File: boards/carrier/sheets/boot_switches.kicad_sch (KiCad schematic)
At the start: 8 parts, among them SW1 DS-04P, SW2 TS-1002S-06026C

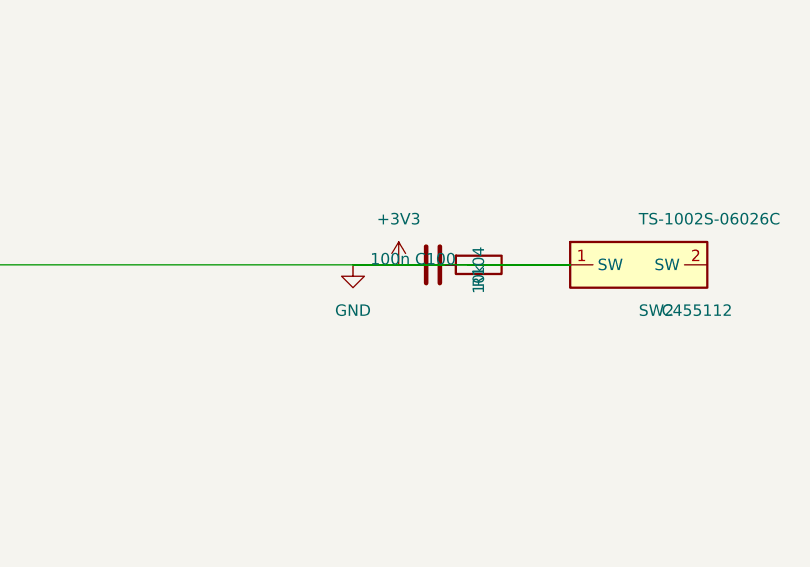
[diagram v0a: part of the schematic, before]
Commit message: Stage 5.5: rotation-derived pin sides + per-edge slot pitch (cluster fix)
Applies the in-flight cluster-fix agent's work (session limit cut its
own commit short). Two architectural changes that close the
sub-sheet wire_dangling / net-merging class of errors:

1) Rotation-derived page-side detection
   (core/layout/geometry.py + core/layout/cluster.py)

   Previously cluster.pin_side() compared abs(pin.x) vs abs(pin.y) on
   the symbol-relative coordinate to guess which body edge a pin
   emerges from. This mis-classified pins on ICs whose pin columns
   span a larger y-range than the body width — FUSB302's seven
   left-column pins (±7.62 mm in y) on a 20 mm-wide body wrap to
   "top/bottom" with the axis-dominance rule, but they're actually
   left-edge pins. The cluster then places passives on the wrong
   side and the resulting wires collide into other nets.

   The new page_side_from_pin() helper derives the page-side from the
   pin's intrinsic KiCad rotation (0 = LEFT edge, 90 = BOTTOM, 180 =
   RIGHT, 270 = TOP) combined with the placed symbol's rotation. This
   is the canonical KiCad convention and doesn't depend on body
   proportions.

   PinGeometry / PinGeometryAbs gain pin_rotation + symbol_rotation
   fields; SymbolGeometryCache reads pin.rotation from the cached
   SymbolDefinition (kicad-sch-api's list_pins() flattens it away).
   pin_side() takes optional pin_rotation/symbol_rotation; falls back
   to the legacy heuristic when not supplied.

2) Per-edge slot pitch
   (core/layout/_constants.py + core/layout/cluster.py)

   LEFT/RIGHT-edge passive swarms fan OUTWARD along the perpendicular
   axis: each slot is one passive body + one power-symbol stub further
   out. The pitch must clear 2 × PASSIVE_PIN_HALF (7.62 mm) +
   POWER_SYMBOL_OFFSET (5.08 mm), so HORIZONTAL_SWARM_PITCH_MM is now
   15.24 mm — was previously the same 5.08 mm used for TOP/BOTTOM, so
   adjacent slots' endpoints collapsed onto one another and KiCad
   merged the entire stack 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
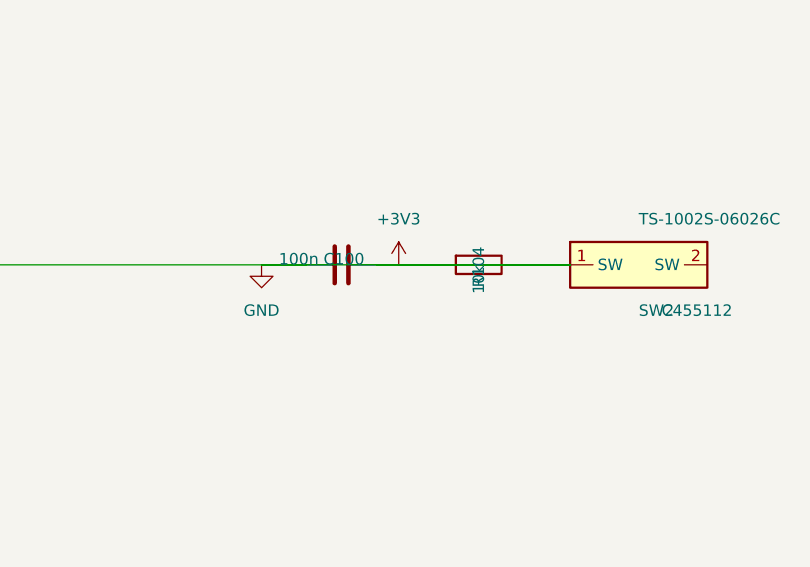
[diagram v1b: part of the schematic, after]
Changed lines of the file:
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@@
 		(instances
 			(project "Boot Mode Straps + PS Reset (DIP-4 + Tactile)"
-				(path "/5430e636-a627-40ff-98cd-1c4e21692bee"
+				(path "/abf145c9-8d90-4f35-b365-cb22af262226"
 					(reference "SW1")
 					(unit 1)
@@
 		(instances
 			(project "Boot Mode Straps + PS Reset (DIP-4 + Tactile)"
-				(path "/5430e636-a627-40ff-98cd-1c4e21692bee"
+				(path "/abf145c9-8d90-4f35-b365-cb22af262226"
 					(reference "R100")
 					(unit 1)
@@
 		(instances
 			(project "Boot Mode Straps + PS Reset (DIP-4 + Tactile)"
-				(path "/5430e636-a627-40ff-98cd-1c4e21692bee"
+				(path "/abf145c9-8d90-4f35-b365-cb22af262226"
 					(reference "#PWR100")
 					(unit 1)
@@
 		(instances
 			(project "Boot Mode Straps + PS Reset (DIP-4 + Tactile)"
-				(path "/5430e636-a627-40ff-98cd-1c4e21692bee"
+				(path "/abf145c9-8d90-4f35-b365-cb22af262226"
 					(reference "R101")
 					(unit 1)
@@
 		(instances
 			(project "Boot Mode Straps + PS Reset (DIP-4 + Tactile)"
-				(path "/5430e636-a627-40ff-98cd-1c4e21692bee"
+				(path "/abf145c9-8d90-4f35-b365-cb22af262226"
 					(reference "#PWR101")
 					(unit 1)
@@
 		(instances
 			(project "Boot Mode Straps + PS Reset (DIP-4 + Tactile)"
-				(path "/5430e636-a627-40ff-98cd-1c4e21692bee"
+				(path "/abf145c9-8d90-4f35-b365-cb22af262226"
 					(reference "R102")
 					(unit 1)
@@
 		(instances
 			(project "Boot Mode Straps + PS Reset (DIP-4 + Tactile)"
-				(path "/5430e636-a627-40ff-98cd-1c4e21692bee"
+				(path "/abf145c9-8d90-4f35-b365-cb22af262226"
 					(reference "#PWR102")
 					(unit 1)
@@
 		(instances
 			(project "Boot Mode Straps + PS Reset (DIP-4 + Tactile)"
-				(path "/5430e636-a627-40ff-98cd-1c4e21692bee"
+				(path "/abf145c9-8d90-4f35-b365-cb22af262226"
 					(reference "R103")
 					(unit 1)
@@
 		(instances
 			(project "Boot Mode Straps + PS Reset (DIP-4 + Tactile)"
-				(path "/5430e636-a627-40ff-98cd-1c4e21692bee"
+				(path "/abf145c9-8d90-4f35-b365-cb22af262226"
 					(reference "#PWR103")
 					(unit 1)
@@
 		(instances
 			(project "Boot Mode Straps + PS Reset (DIP-4 + Tactile)"
-				(path "/5430e636-a627-40ff-98cd-1c4e21692bee"
+				(path "/abf145c9-8d90-4f35-b365-cb22af262226"
 					(reference "SW2")
 					(unit 1)
@@
 		(instances
 			(project "Boot Mode Straps + PS Reset (DIP-4 + Tactile)"
-				(path "/5430e636-a627-40ff-98cd-1c4e21692bee"
+				(path "/abf145c9-8d90-4f35-b365-cb22af262226"
 					(reference "R104")
 					(unit 1)
@@
 		(instances
 			(project "Boot Mode Straps + PS Reset (DIP-4 + Tactile)"
-				(path "/5430e636-a627-40ff-98cd-1c4e21692bee"
+				(path "/abf145c9-8d90-4f35-b365-cb22af262226"
 					(reference "#PWR104")
 					(unit 1)
@@
 	(symbol
 		(lib_id "Device:C")
-		(at 106.68 105.41 270)
+		(at 96.52 105.41 270)
 		(unit 1)
 		(exclude_from_sim no)
@@
 		(fields_autoplaced no)
 		(property "Reference" "C100"
-			(at 109.22 104.775 270)
+			(at 99.06 104.775 270)
 			(effects
 				(font
@@
 		)
 		(property "Value" "100n"
-			(at 104.14 104.775 270)
+			(at 93.98 104.775 270)
 			(effects
 				(font
@@
 		)
 		(property "Footprint" "Capacitor_SMD:C_0402_1005Metric"
-			(at 107.6452 101.6 0.0000)
+			(at 97.4852 101.6 0.0000)
 			(effects
 				(font
@@
 		(instances
 			(project "Boot Mode Straps + PS Reset (DIP-4 + Tactile)"
-				(path "/5430e636-a627-40ff-98cd-1c4e21692bee"
+				(path "/abf145c9-8d90-4f35-b365-cb22af262226"
 					(reference "C100")
 					(unit 1)
@@
 	(symbol
 		(lib_id "power:GND")
-		(at 97.79 105.41 0)
+		(at 87.63 105.41 0)
 		(unit 1)
 		(exclude_from_sim no)
@@
 		(fields_autoplaced no)
 		(property "Reference" "#PWR105"
-			(at 97.79 99.06 0.0000)
+			(at 87.63 99.06 0.0000)
 			(effects
 				(font
@@
 		)
 		(property "Value" "GND"
-			(at 97.79 110.49 0)
+			(at 87.63 110.49 0)
 			(effects
 				(font
@@
 		)
 		(property "Footprint" ""
-			(at 97.79 105.41 0.0000)
-			(effects
-				(font
-					(size 1.27 1.27)
-				)
-				(hide yes)
-			)
-		)
-		(pin "1"
-		)
-		(instances
-			(project "Boot Mode Straps + PS Reset (DIP-4 + Tactile)"
-				(path "/5430e636-a627-40ff-98cd-1c4e21692bee"
+			(at 87.63 105.41 0.0000)
+			(effects
+				(font
+					(size 1.27 1.27)
+				)
+				(hide yes)
+			)
+		)
+		(pin "1"
+		)
+		(instances
+			(project "Boot Mode Straps + PS Reset (DIP-4 + Tactile)"
+				(path "/abf145c9-8d90-4f35-b365-cb22af262226"
 					(reference "#PWR105")
 					(unit 1)
@@
 		(instances
 			(project "Boot Mode Straps + PS Reset (DIP-4 + Tactile)"
-				(path "/5430e636-a627-40ff-98cd-1c4e21692bee"
+				(path "/abf145c9-8d90-4f35-b365-cb22af262226"
 					(reference "#PWR106")
 					(unit 1)
@@
 	(wire
 		(pts
-			(xy 121.92 105.41) (xy 110.49 105.41)
-		)
-		(stroke
-			(width 0)
-			(type default)
-		)
-	)
-	(wire
-		(pts
-			(xy 102.87 105.41) (xy 97.79 105.41)
-		)
-		(stroke
+			(xy 121.92 105.41) (xy 100.33 105.41)
+		)
+		(stroke
+			(width 0)
+			(type default)
+		)
+	)
+	(wire
+		(pts
+			(xy 92.71 105.41) (xy 87.63 105.41)
+		)
+		(stroke
